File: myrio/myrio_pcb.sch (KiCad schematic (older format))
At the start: 126 parts, among them J1 CONN_02X03, J2 CONN_02X03, J3 CONN_02X03, J4 CONN_02X03, P1 CONN_02X17, P2 CONN_02X17, Q1 PN2222A, Q10 PN2222A, Q11 PN2222A, Q12 PN2222A, Q13 PN2222A, Q14 PN2222A, Q15 PN2222A, Q16 PN2222A, Q17 PN2222A, Q18 PN2222A, Q19 PN2222A, Q2 PN2222A, Q20 PN2222A, Q3 PN2222A, Q4 PN2222A, Q5 PN2222A, Q6 PN2222A, Q7 PN2222A, Q8 PN2222A, Q9 PN2222A, U1 stacked-DB9, U10 INA219, U11 INA219, U13 INA219, U14 stacked-rj45-LED, U15 stacked-rj45-LED, U2 stacked-DB9, U3 stacked-rj45-LED, U4 stacked-rj45-LED, U5 stacked-rj45-LED, U6 BNO055, U7 stacked-rj45-LED, U8 stacked-DB9

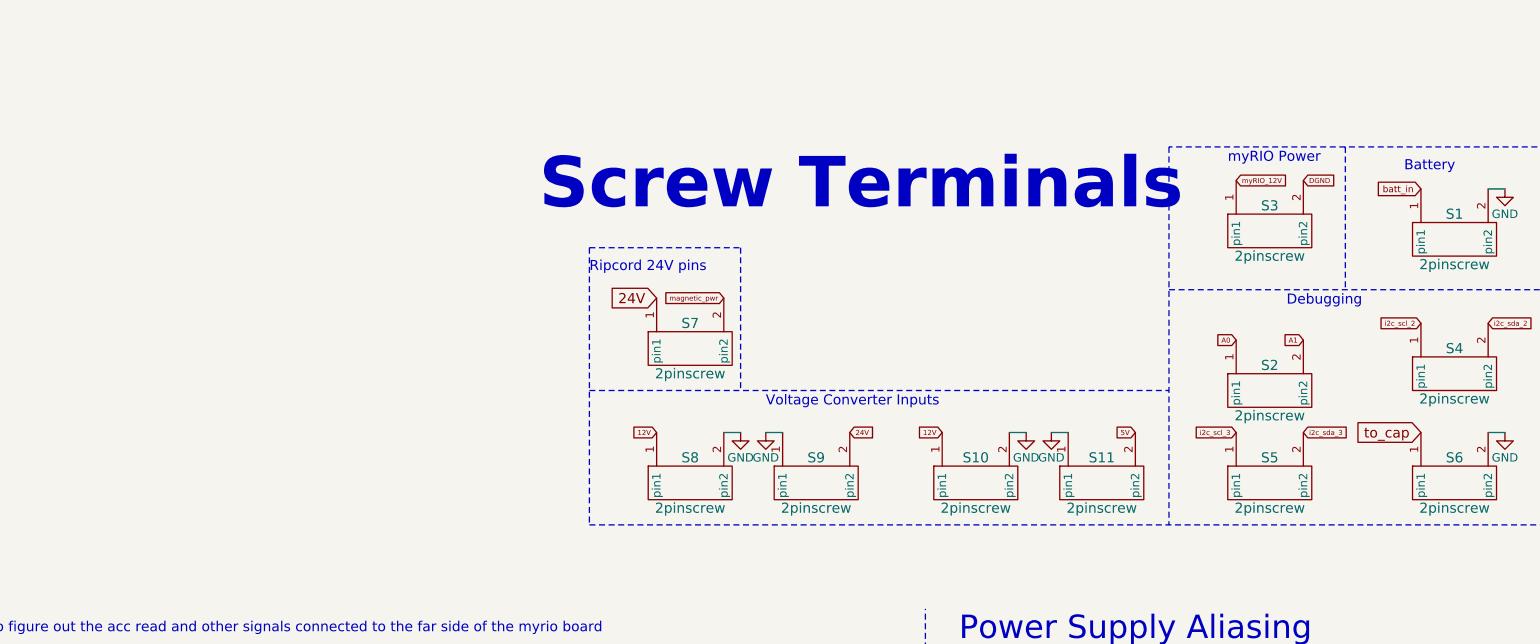
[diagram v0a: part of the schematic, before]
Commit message: made the battery fuse
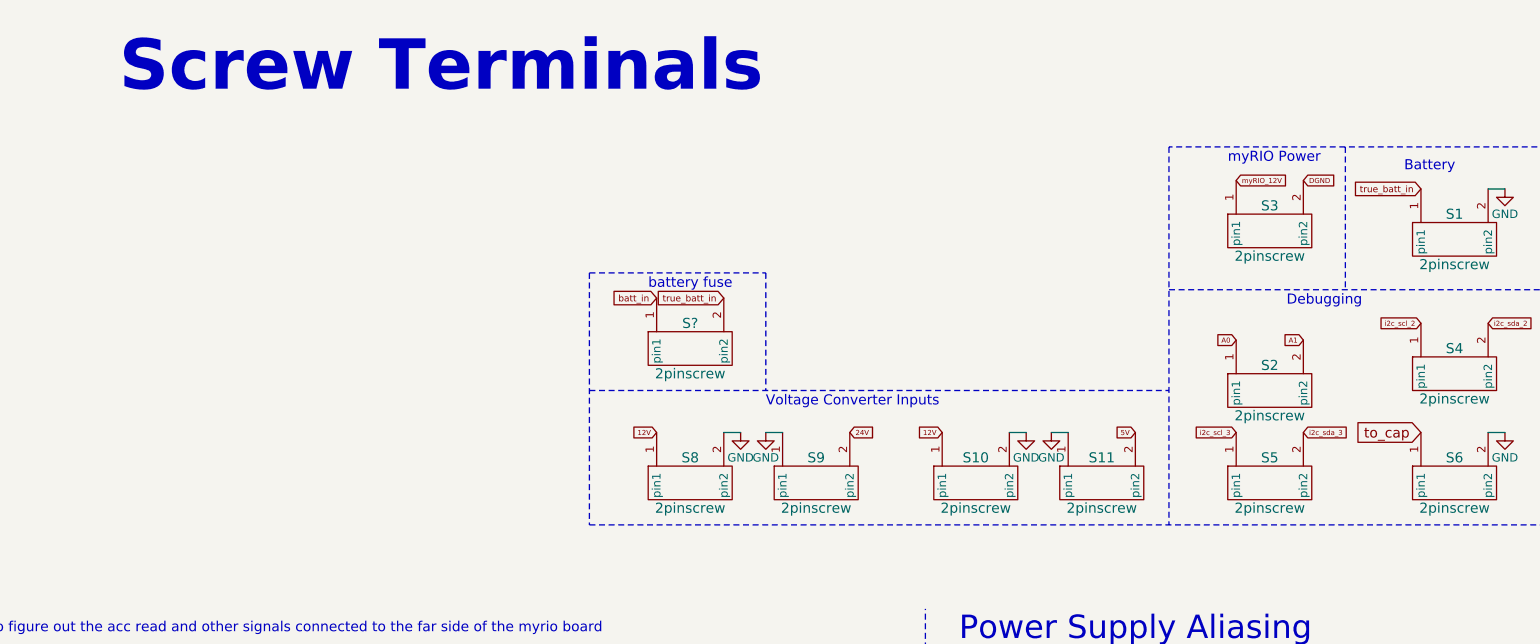
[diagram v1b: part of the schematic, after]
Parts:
- removed S7: 2pinscrew, footprints:screwinconnector++, symbol 2pinscrew
- added S?: 2pinscrew, footprints:screwinconnector++, symbol 2pinscrew
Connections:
- net batt_in: now also S?.1 (pin1); no longer S1.1 (pin1)
- new net true_batt_in: S1.1 (pin1), S?.2 (pin2)
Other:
- note added: "battery fuse"
- note removed: "Ripcord 24V pins"
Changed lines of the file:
@@
 Text GLabel 9050 3050 2    30   Input ~ 0
 non_critical_sda
-Text GLabel 9250 -2000 0    39   Input ~ 0
+Text GLabel 4700 -1350 0    39   Input ~ 0
 batt_in
 Text GLabel 9050 3150 2    30   Input ~ 0
@@
 Text GLabel 8000 1400 1    30   Input ~ 0
 24V
-$Comp
-L 2pinscrew S7
-U 1 1 5935F3F1
-P 4900 -1300
-F 0 "S7" H 4900 -1400 60  0000 C CNN
-F 1 "2pinscrew" H 4900 -1700 60  0000 C CNN
-F 2 "footprints:screwinconnector++" H 4900 -1300 60  0001 C CNN
-F 3 "" H 4900 -1300 60  0001 C CNN
-	1    4900 -1300
-	1    0    0    -1
-$EndComp
-Text GLabel 4700 -1350 0    60   Input ~ 0
-24V
-Text Notes 4300 -1500 0    60   ~ 0
-Ripcord 24V pins
 Text GLabel 7350 1550 0    30   Input ~ 0
 12V
@@
 Connection ~ 8000 1500
 Wire Notes Line
-	4300 -1650 4300 0
-Wire Notes Line
 	4300 -800 7750 -800
 Wire Notes Line
@@
 Wire Notes Line
 	4300 0    10000 0
-Wire Notes Line
-	4300 -1650 5200 -1650
-Wire Notes Line
-	5200 -1650 5200 -800
 Text Notes 8450 -1300 0    60   ~ 0
 Debugging
@@
 Wire Notes Line
 	8800 -2250 8800 -1400
-Text Notes 4000 -1850 0    300  ~ 60
+Text Notes 1500 -2550 0    300  ~ 60
 Screw Terminals
 Text GLabel 4700 -550 0    30   Input ~ 0
@@
 Wire Notes Line
 	6500 12600 700  12600
-Text GLabel 5100 -1350 0    30   Input ~ 0
-magnetic_pwr
 Wire Wire Line
 	5450 -550 5350 -550
@@
 NoConn ~ -250 11100
 NoConn ~ -250 11600
+Wire Notes Line
+	4300 -1500 4300 0
+$Comp
+L 2pinscrew S?
+U 1 1 5970737F
+P 4900 -1300
+F 0 "S?" H 4900 -1400 60  0000 C CNN
+F 1 "2pinscrew" H 4900 -1700 60  0000 C CNN
+F 2 "footprints:screwinconnector++" H 4900 -1300 60  0001 C CNN
+F 3 "" H 4900 -1300 60  0001 C CNN
+	1    4900 -1300
+	1    0    0    -1
+$EndComp
+Text GLabel 9250 -2000 0    39   Input ~ 0
+true_batt_in
+Text GLabel 5100 -1350 0    39   Input ~ 0
+true_batt_in
+Text Notes 4650 -1400 0    60   ~ 0
+battery fuse
+Wire Notes Line
+	4300 -1500 5350 -1500
+Wire Notes Line
+	5350 -1500 5350 -800
 $EndSCHEMATC

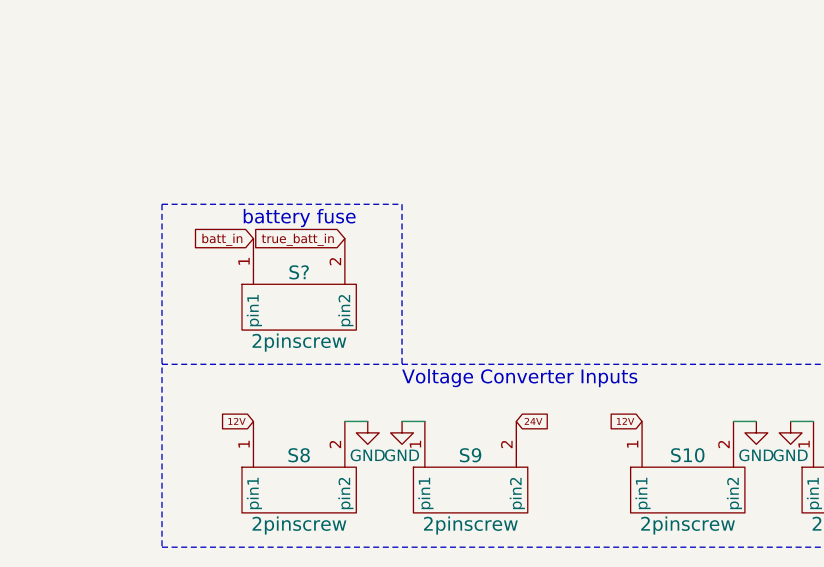
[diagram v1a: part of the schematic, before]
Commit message: made the router screw terminal
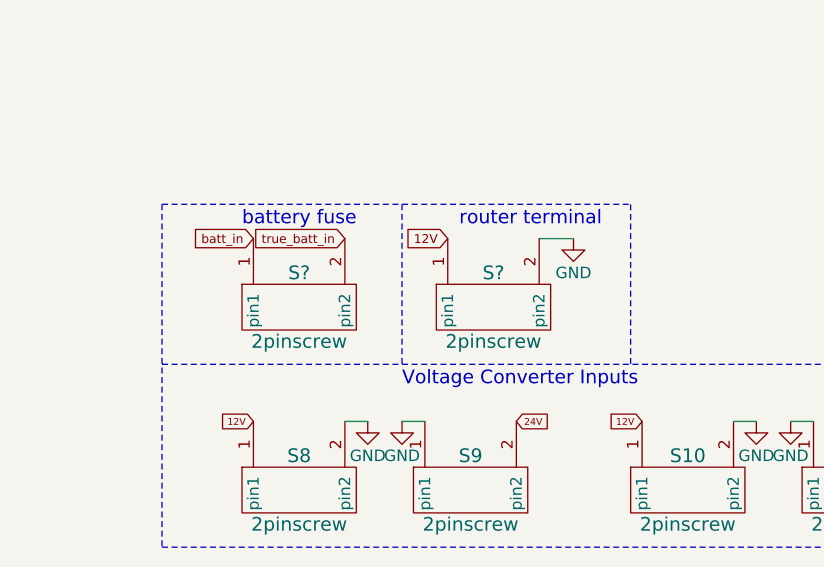
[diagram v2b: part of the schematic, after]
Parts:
- added S?: 2pinscrew, footprints:screwinconnector++, symbol 2pinscrew
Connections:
- net 12V: now also S?.1 (pin1)
- net GND: now also S?.2 (pin2)
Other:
- note added: "router terminal"
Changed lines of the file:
@@
 battery fuse
 Wire Notes Line
-	4300 -1500 5350 -1500
+	4300 -1500 6350 -1500
 Wire Notes Line
 	5350 -1500 5350 -800
+$Comp
+L 2pinscrew S?
+U 1 1 5970A4EC
+P 5750 -1300
+F 0 "S?" H 5750 -1400 60  0000 C CNN
+F 1 "2pinscrew" H 5750 -1700 60  0000 C CNN
+F 2 "footprints:screwinconnector++" H 5750 -1300 60  0001 C CNN
+F 3 "" H 5750 -1300 60  0001 C CNN
+	1    5750 -1300
+	1    0    0    -1
+$EndComp
+$Comp
+L GND #PWR?
+U 1 1 5970A700
+P 6100 -1350
+F 0 "#PWR?" H 6100 -1600 50  0001 C CNN
+F 1 "GND" H 6100 -1500 50  0000 C CNN
+F 2 "" H 6100 -1350 50  0001 C CNN
+F 3 "" H 6100 -1350 50  0001 C CNN
+	1    6100 -1350
+	1    0    0    -1
+$EndComp
+Wire Wire Line
+	5950 -1350 6100 -1350
+Text GLabel 5550 -1350 0    39   Input ~ 0
+12V
+Text Notes 5600 -1400 0    60   ~ 0
+router terminal
+Wire Notes Line
+	6350 -1500 6350 -800
 $EndSCHEMATC

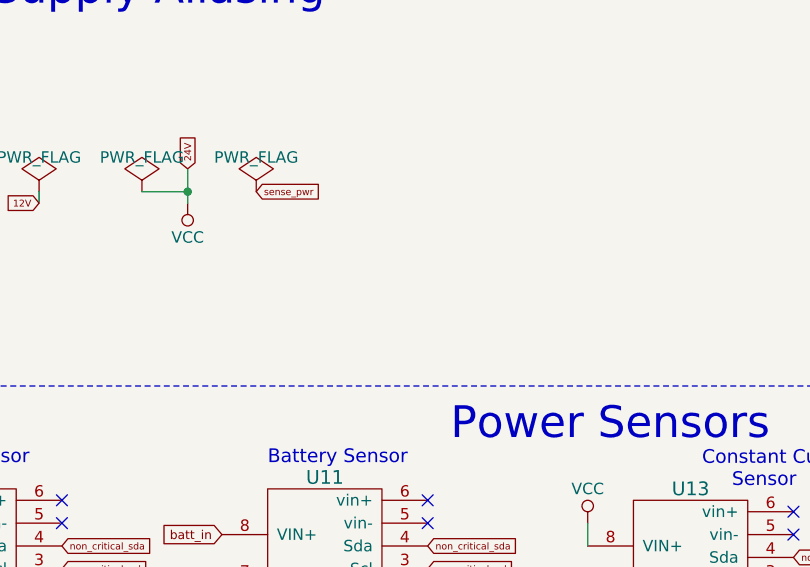
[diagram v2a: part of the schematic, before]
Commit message: added the LED haven't connected it to the switch yet
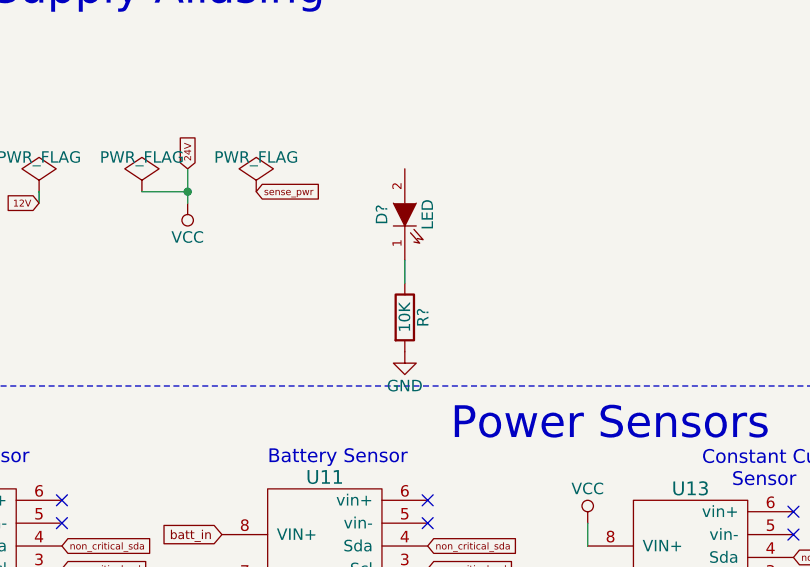
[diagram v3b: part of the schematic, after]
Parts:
- added D?: LED, symbol LED
- added R?: 10K, symbol R
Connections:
- net GND: now also R?.2
- new net: D?.1 (K), R?.1
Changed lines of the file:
@@
 Wire Notes Line
 	6350 -1500 6350 -800
+$Comp
+L LED D?
+U 1 1 596FFCA6
+P 8950 1600
+F 0 "D?" H 8950 1700 50  0000 C CNN
+F 1 "LED" H 8950 1500 50  0000 C CNN
+F 2 "" H 8950 1600 50  0000 C CNN
+F 3 "" H 8950 1600 50  0000 C CNN
+	1    8950 1600
+	0    -1   -1   0
+$EndComp
+$Comp
+L R R?
+U 1 1 597018D1
+P 8950 2050
+F 0 "R?" V 9030 2050 50  0000 C CNN
+F 1 "10K" V 8950 2050 50  0000 C CNN
+F 2 "" V 8880 2050 50  0000 C CNN
+F 3 "" H 8950 2050 50  0000 C CNN
+	1    8950 2050
+	1    0    0    -1
+$EndComp
+Wire Wire Line
+	8950 1900 8950 1800
+$Comp
+L GND #PWR?
+U 1 1 59701D82
+P 8950 2200
+F 0 "#PWR?" H 8950 1950 50  0001 C CNN
+F 1 "GND" H 8950 2050 50  0000 C CNN
+F 2 "" H 8950 2200 50  0000 C CNN
+F 3 "" H 8950 2200 50  0000 C CNN
+	1    8950 2200
+	1    0    0    -1
+$EndComp
 $EndSCHEMATC

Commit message: updated the schematic
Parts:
- added S?: L101011MS02Q, symbol L101011MS02Q
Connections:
- net batt_in: now also D?.2 (A), S?.1 (SideA); no longer S?.1 (pin1)
- new net fuse_to_switch: S?.1 (pin1), S?.2 (SideB)
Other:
- note added: "i think i accidentally wrote 10k think its supposed to be 1k"
- moved on the sheet: D?, R?

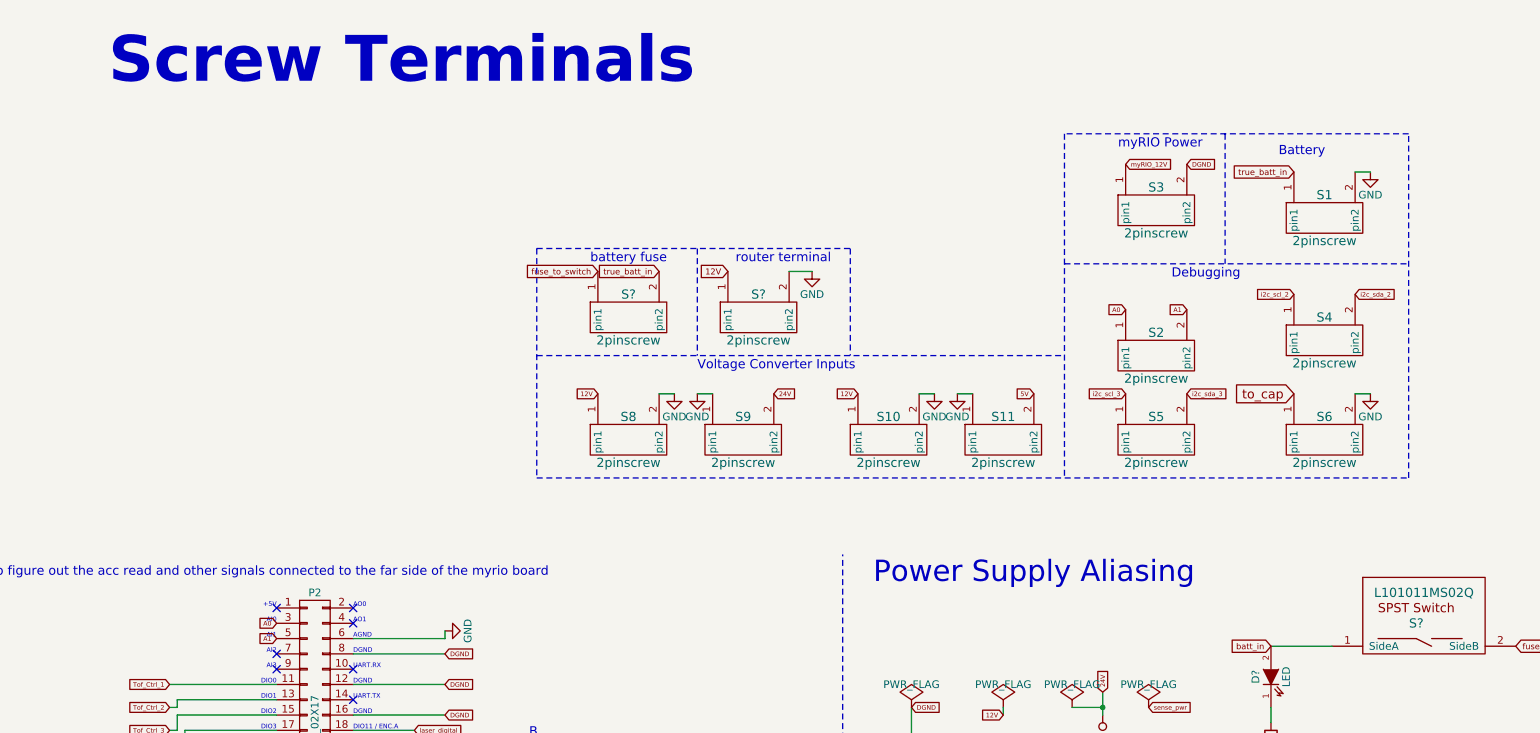
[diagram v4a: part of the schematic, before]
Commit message: made the screw terminal changes
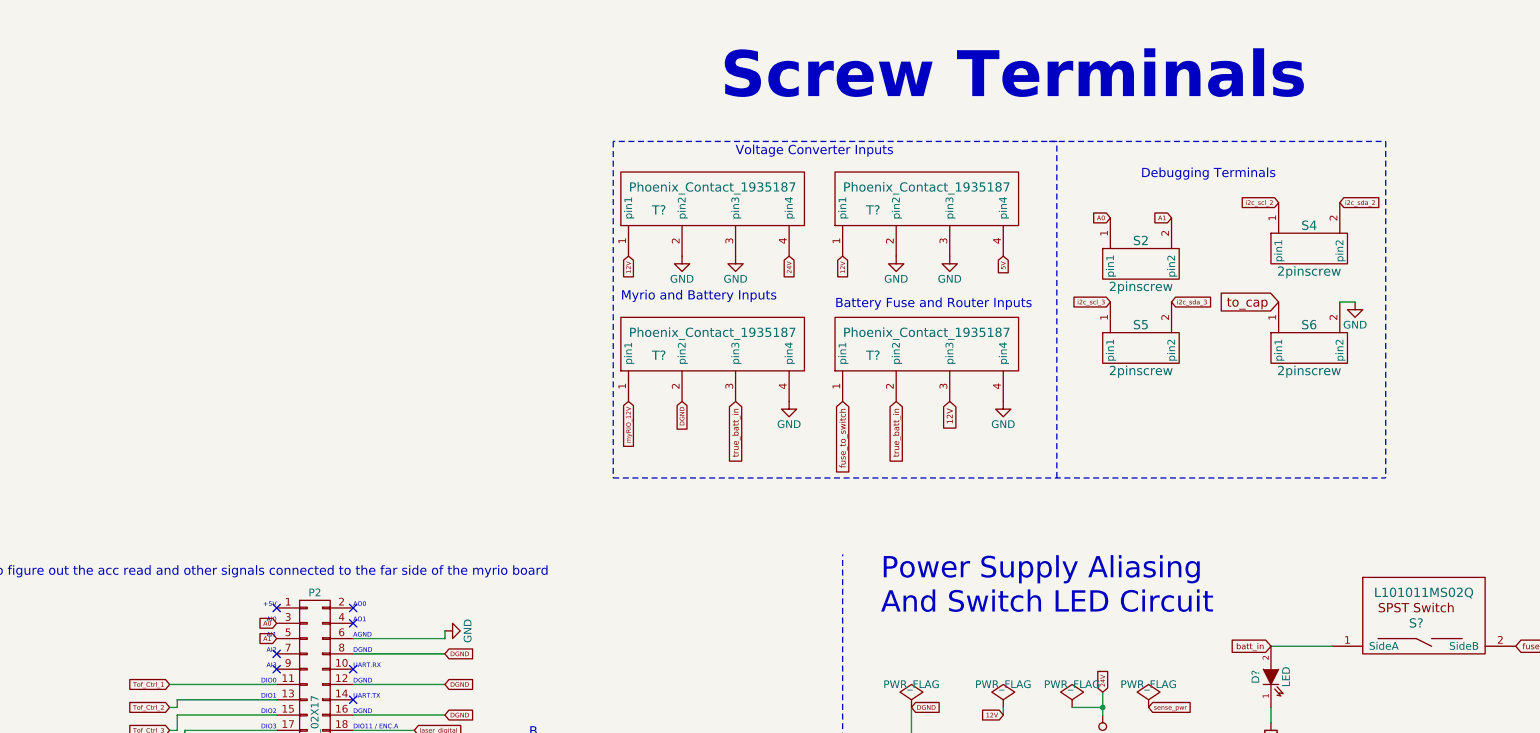
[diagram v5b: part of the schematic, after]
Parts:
- removed S1, S10, S11, S3, S8, S9, S? (x2): 2pinscrew, footprints:screwinconnector++, symbol 2pinscrew
- added T? (x4): Phoenix_Contact_1935187, symbol Phoenix_Contact_1935187
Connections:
- net 12V: now also T?.1 (pin1), T?.1 (pin1), T?.3 (pin3)
- net 5V: now also T?.4 (pin4)
- net GND: now also T?.2 (pin2), T?.2 (pin2), T?.2 (pin2), T?.3 (pin3), T?.3 (pin3), T?.4 (pin4), T?.4 (pin4)
- net VCC: now also T?.4 (pin4)
- net fuse_to_switch: now also T?.1 (pin1)
- net myRIO_12V: now also T?.1 (pin1)
- net true_batt_in: now also T?.2 (pin2), T?.3 (pin3)
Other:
- note added: "Battery Fuse and Router Inputs"
- note added: "Debugging Terminals"
- note added: "Myrio and Battery Inputs"
- note added: "Power Supply Aliasing\nAnd Switch LED Circuit"
- note removed: "Battery"
- note removed: "Debugging"
- note removed: "Power Supply Aliasing"
- note removed: "battery fuse"
- note removed: "myRIO Power"
- note removed: "router terminal"
- moved on the sheet: S2, S4, S5, S6
